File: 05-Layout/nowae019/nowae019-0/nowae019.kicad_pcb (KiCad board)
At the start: 2 copper layers, 55 x 30 mm, 4 parts, among them P1 U-MULTILINK-SMALL, P2 U-MULTILINK, P3 TAG, P4 CUSTOM

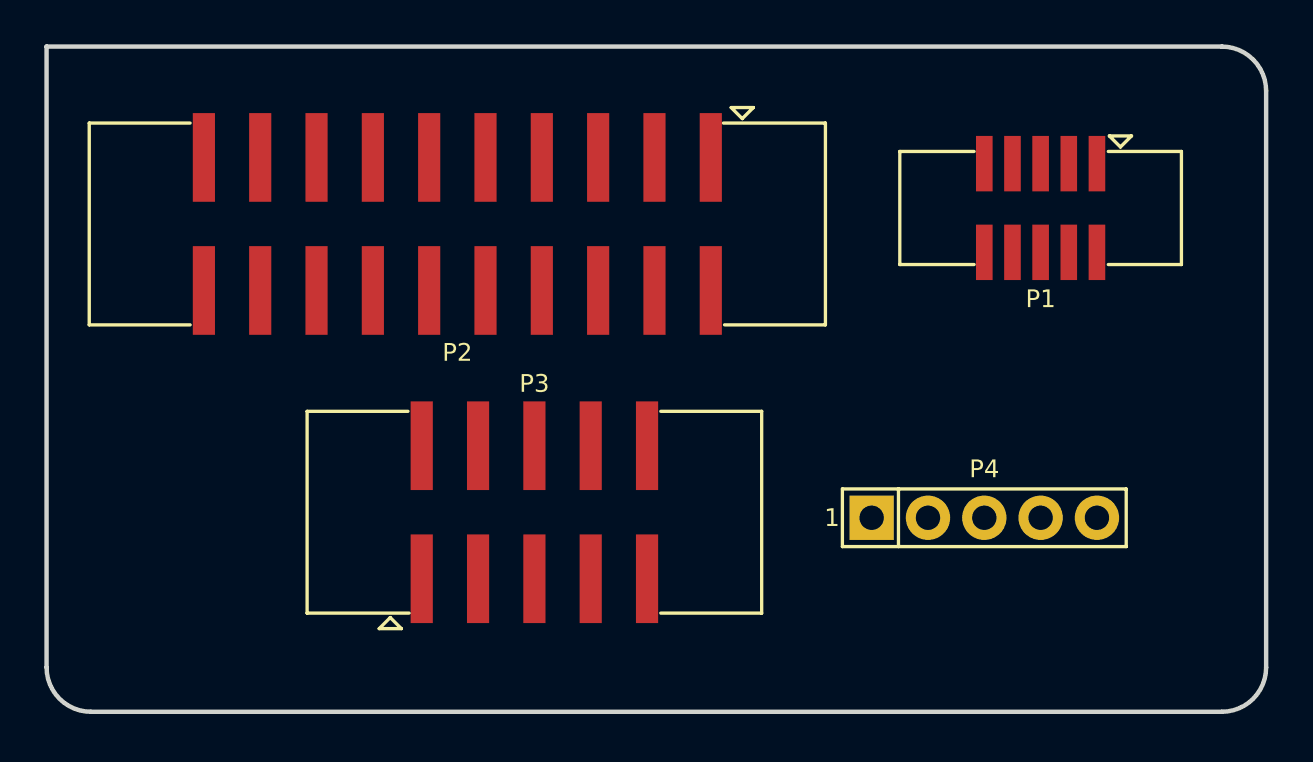
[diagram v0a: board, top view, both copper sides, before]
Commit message: Added NOWAE logo (nowae019-0)
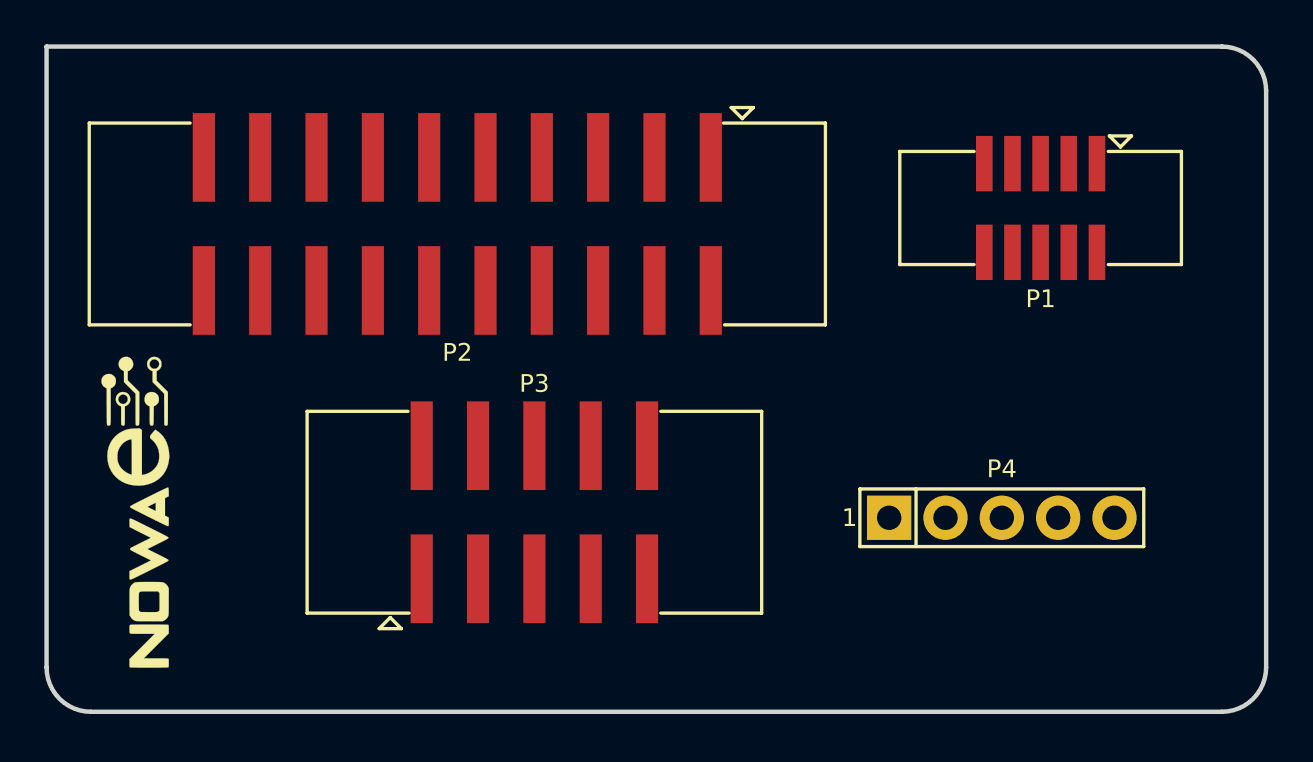
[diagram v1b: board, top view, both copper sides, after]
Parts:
- added G***: LOGO, LOGO:LOGO_NOWAE_15MM_FSILK, F.Cu at (123.0, 95.0)
- moved P4 0.79 mm to (162.1, 95.2)

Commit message: Started routing (nowae019-0)
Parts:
- moved P4 1.77 mm to (163.8, 95.3)
- moved G*** 0.92 mm to (122.3, 95.7)
- turned P1 to 0 degrees
- turned P2 to 0 degrees
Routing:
- net /PROG_GND: track 0.00 -> 62.0 mm
- net /PROG_VCC: track 0.00 -> 60.6 mm
- net /PROG_TDI: track 0.00 -> 51.4 mm
- net /PROG_RESET: track 0.00 -> 25.0 mm
- net /PROG_SWDIO: track 0.00 -> 9.41 mm
- net /PROG_SWCLK: track 0.00 -> 7.91 mm
- net /PROG_SW0: track 0.00 -> 7.14 mm
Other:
- net class Default: trace_width 0.25 -> 0.2
- rule via_min_drill: 0.3 -> 0.4
- rule via_min_size: 0.4 -> 0.8

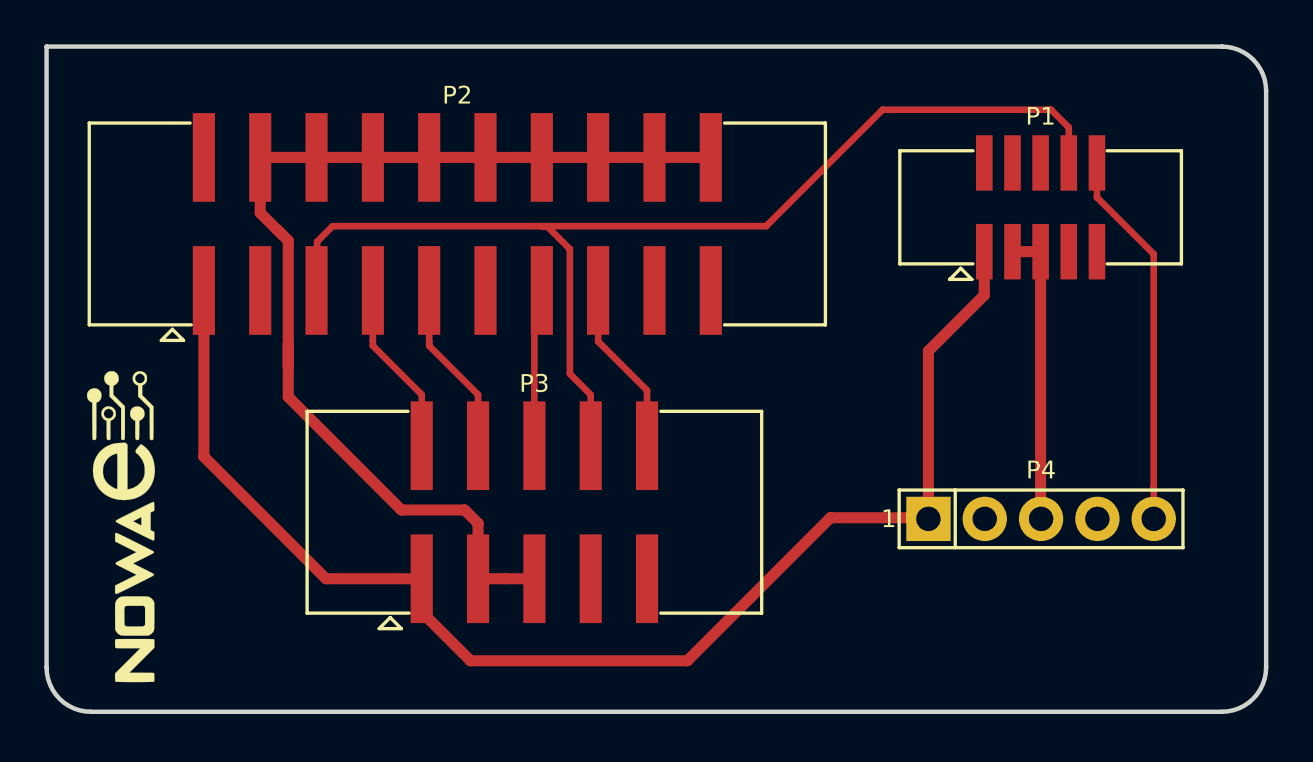
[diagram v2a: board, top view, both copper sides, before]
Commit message: Ended routing. Added logos and silkscreen informations. (nowae019-0)
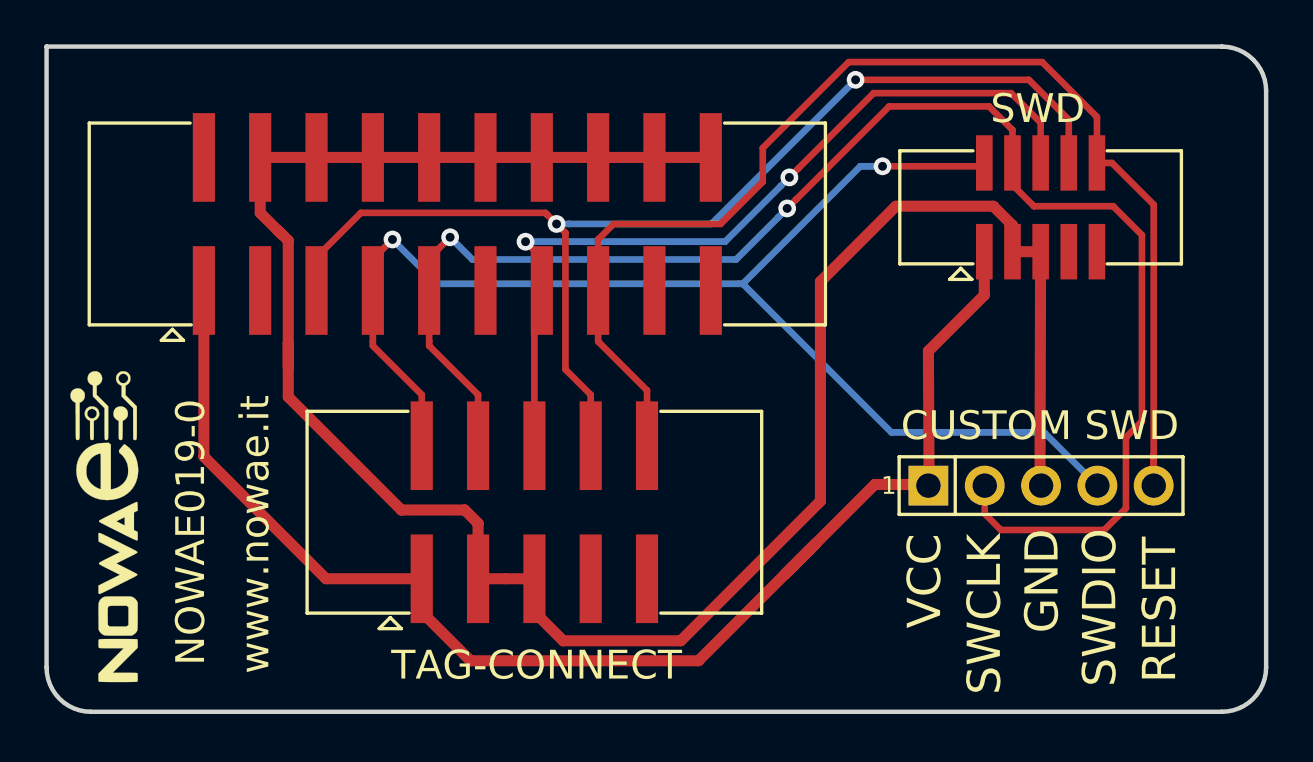
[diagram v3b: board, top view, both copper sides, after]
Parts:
- added G***: LOGO, EXTLOGO:LOGO_CC-BY-SA_10MM_FSILK, B.Cu at (149.0, 96.5)
- added G***: LOGO, EXTLOGO:LOGO_OSH_10MM_FSILK, B.Cu at (149.0, 81.5)
- added G***: LOGO, LOGO:LOGO_NOWAE_30MM_FSILK, B.Cu at (134.4, 89.0)
- moved P4 1.50 mm to (163.8, 93.8)
- moved G*** 0.75 mm to (121.6, 95.7)
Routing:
- net /PROG_SWCLK: track 7.91 -> 70.0 mm, vias 0 -> 2
- net /PROG_SWDIO: track 9.41 -> 61.6 mm, vias 0 -> 2
- net /PROG_GND: track 62.0 -> 99.7 mm
- net /PROG_RESET: track 25.0 -> 57.5 mm
- net /PROG_SW0: track 7.14 -> 38.0 mm, vias 0 -> 2
- net /PROG_VCC: track 60.6 -> 61.7 mm
- net /PROG_TDI: track 51.4 -> 52.5 mm, vias 0 -> 2
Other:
- board text added: "CUSTOM SWD"
- board text added: "GND"
- board text added: "NOWAE019-0"
- board text added: "RESET"
- board text added: "SWCLK"
- board text added: "SWD"
- board text added: "SWDIO"
- board text added: "TAG-CONNECT"
- board text added: "U-Multilink Adapter NOWAE019-0"
- board text added: "VCC"
- board text added: "designed by"
- board text added: "www.nowae.it"
